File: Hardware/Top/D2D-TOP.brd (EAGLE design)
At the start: 38 x 38 mm, 54 parts, among them SW1 SWITCH.MOM, SW2 SWITCH.MOM, U2 NRF52832_MODULE_MDBT42, U4 PCF8523, U6 PHOTOTRANSISTOR

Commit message: current top and bottom board
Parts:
- added SW5: SWITCH.MOM, LinnesLab-Switches:TACTILE_SWITCH_SMD_6.2MM_TALL
- moved C16 18.7 mm to (9.37, 21.7)
- moved U4 13.0 mm to (7.32, 15.8)
- moved XTAL3 11.8 mm to (5.33, 21.4)
- moved C2 11.1 mm to (5.28, 24.8), turned to 91.7 degrees
- moved C18 11.0 mm to (13.1, 23.7)
- moved L2 10.9 mm to (10.2, 26.1)
- moved C17 10.5 mm to (5.23, 31.8)
- moved C12 10.3 mm to (12.7, 20.4)
- moved C4 10.0 mm to (8.31, 28.4)
- moved C7 10.0 mm to (12.7, 27.5)
- moved C19 6.95 mm to (5.28, 28.1)
- moved R16 5.59 mm to (12.4, 30.0)
- moved U6 5.27 mm to (12.9, 33.0)
- moved C5 5.10 mm to (9.14, 2.97)
- moved R8 4.65 mm to (7.47, 32.2)
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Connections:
- net VBATT renamed VBAT
- net GND: now also SW5.B1, SW5.B2, USB2.S1, USB2.S2, USB2.S3, USB2.S4, USB2.S5, USB2.S6
- net SW1: now also SW5.A1

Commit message: unfinished 002
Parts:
- removed SW5: SWITCH.MOM, LinnesLab-Switches:TACTILE_SWITCH_SMD_6.2MM_TALL
- added C23: 100n, LinnesLab-Passives:C0603
- added C24, C25: 47p, LinnesLab-Passives:C0603
- added J1: (no value), LinnesLab-Connectors:1X07
- added JP2: (no value), LinnesLab-Switches:SMT-JUMPER_2_NO_SILK
- added LED5: RED, LinnesLab-LED:LED-0603
- added LED6: YELLOW, LinnesLab-LED:LED-0603
- added R1, R2: 0, LinnesLab-Passives:R0603
- added R18, R19: 27, LinnesLab-Passives:R0603
- added R20, R21: 1k, LinnesLab-Passives:R0603
- added U5: FT231XS, LinnesLab-DigitalIC:SSOP20_L
- R9: value 10k -> (none)
- moved R9 45.8 mm to (-3.58, -11.9), turned to 0 degrees
- moved R8 42.8 mm to (-3.58, -9.17), turned to 0 degrees
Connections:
- removed net BATT: R13.1, R14.2
- removed net CHRG.STAT: CHRG2.1, R12.1
- removed net RXD: U2.21
- removed net TXD: U2.19
- new net A4/BATT: R13.1, R14.2, U2.5
- new net CTS: JP2.2, U5.9
- new net D27/CHRGSTATUS: CHRG2.1, R12.1, U2.4
- new net FT3V3: U5.13
- new net N$23: R18.2, U5.12
- new net N$24: R19.2, U5.11
- new net N$25: LED5.C, R20.2
- new net N$26: LED6.C, R21.2
- new net RXD.FT: R2.1, U5.4
- new net RXD.NRF: R1.2, U2.21
- new net RXLED: R20.1, U5.17
- new net TXD.FT: R1.1, U5.20
- new net TXD.NRF: R2.2, U2.19
- new net TXLED: R21.1, U5.10
- net 3.3V: now also C23.2, LED5.A, LED6.A, U5.14, U5.3
- net DTR: now also U5.1
- net GND: now also C23.1, C24.2, C25.1, JP2.1, U5.16, U5.6; no longer SW5.B1, SW5.B2
- net SCL: now also R9.1; no longer R8.1
- net SDA: now also R8.1; no longer R9.1
- net SW1: no longer SW5.A1
- net USB+: now also C24.1, R19.1
- net USB-: now also C25.2, R18.1
- net V_USB: now also U5.15

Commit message: updated to 002
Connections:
- removed net CD1: SD2.CD1
- removed net CS.OLED: U3.13
- removed net DC.OLED: U3.15
- removed net RESET.OLED: U3.14
- removed net SD.CS: SD2.2
- removed net SW1: SW1.A1, SW2.A1
- new net A6/TIA: J1.5, U2.7
- new net A7/PPG: J1.7, U2.8
- new net D11/SW1: SW1.A1, U2.25
- new net D15/SW2: SW2.A1, U2.29
- new net D16/CS.OLED: U2.30, U3.13
- new net D29/LED.CTRL: J1.6, U2.6
- new net D3/RESET.OLED: U2.16, U3.14
- new net D4/DC.OLED: U2.17, U3.15
- new net D5/CD1: SD2.CD1, U2.18
- new net D7/SD.CS: SD2.2, U2.20
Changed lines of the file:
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@@
 <contactref element="U2" pad="38"/>
-</signal>
-<signal name="DC.OLED">
-<contactref element="U3" pad="15"/>
-</signal>
-<signal name="RESET.OLED">
-<contactref element="U3" pad="14"/>
 </signal>
 <signal name="N$1">
@@
 <wire x1="17.1766" y1="31.799" x2="13.0556" y2="24.3228" width="0" layer="19" extent="1-1"/>
 </signal>
-<signal name="CS.OLED">
-<contactref element="U3" pad="13"/>
-</signal>
 <signal name="CD2">
 <contactref element="SD2" pad="CD2"/>
-</signal>
-<signal name="CD1">
-<contactref element="SD2" pad="CD1"/>
-</signal>
-<signal name="SD.CS">
-<contactref element="SD2" pad="2"/>
 </signal>
 <signal name="N$17">
@@
 <wire x1="7.4558" y1="28.3972" x2="11.5706" y2="30.0482" width="0" layer="19" extent="1-1"/>
 </signal>
-<signal name="SW1">
-<contactref element="SW1" pad="A1"/>
-<contactref element="SW2" pad="A1"/>
-<wire x1="28.0798" y1="2.0426" x2="27.8766" y2="8.6466" width="0" layer="19" extent="1-1"/>
-</signal>
 <signal name="VBAT">
 <contactref element="U4" pad="3"/>
@@
 <wire x1="7.3406" y1="8.9272" x2="10.033" y2="7.1002" width="0" layer="19" extent="1-1"/>
 </signal>
+<signal name="D7/SD.CS">
+<contactref element="U2" pad="20"/>
+<contactref element="SD2" pad="2"/>
+<wire x1="31.2204" y1="7.3908" x2="32.007" y2="20.8488" width="0" layer="19" extent="1-16"/>
+</signal>
+<signal name="D5/CD1">
+<contactref element="U2" pad="18"/>
+<contactref element="SD2" pad="CD1"/>
+<wire x1="21.4204" y1="13.2908" x2="30.607" y2="20.8488" width="0" layer="19" extent="1-16"/>
+</signal>
+<signal name="D11/SW1">
+<contactref element="U2" pad="25"/>
+<contactref element="SW1" pad="A1"/>
+<wire x1="28.0798" y1="2.0426" x2="35.207" y2="22.2988" width="0" layer="19" extent="1-1"/>
+</signal>
+<signal name="D15/SW2">
+<contactref element="U2" pad="29"/>
+<contactref element="SW2" pad="A1"/>
+<wire x1="27.8766" y1="8.6466" x2="35.207" y2="25.0988" width="0" layer="19" extent="1-1"/>
+</signal>
+<signal name="D16/CS.OLED">
+<contactref element="U2" pad="30"/>
+<contactref element="U3" pad="13"/>
+<wire x1="17.1766" y1="21.999" x2="35.207" y2="25.7988" width="0" layer="19" extent="1-1"/>
+</signal>
+<signal name="D4/DC.OLED">
+<contactref element="U2" pad="17"/>
+<contactref element="U3" pad="15"/>
+<wire x1="17.1766" y1="23.399" x2="29.907" y2="20.8488" width="0" layer="19" extent="1-1"/>
+</signal>
+<signal name="D3/RESET.OLED">
+<contactref element="U2" pad="16"/>
+<contactref element="U3" pad="14"/>
+<wire x1="17.1766" y1="22.699" x2="29.207" y2="20.8488" width="0" layer="19" extent="1-1"/>
+</signal>
+<signal name="D29/LED.CTRL">
+<contactref element="U2" pad="6"/>
+<contactref element="J1" pad="6"/>
+<wire x1="17.7" y1="33" x2="26.007" y2="26.4988" width="0" layer="19" extent="1-1"/>
+</signal>
+<signal name="A6/TIA">
+<contactref element="U2" pad="7"/>
+<contactref element="J1" pad="5"/>
+<wire x1="15.16" y1="33" x2="26.007" y2="25.7988" width="0" layer="19" extent="1-1"/>
+</signal>
+<signal name="A7/PPG">
+<contactref element="U2" pad="8"/>
+<contactref element="J1" pad="7"/>
+<wire x1="20.24" y1="33" x2="26.007" y2="25.0988" width="0" layer="19" extent="1-1"/>
+</signal>
 </signals>

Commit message: checkpoint 3
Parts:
- removed CHRG2: MCP73831, LinnesLab-Power:SOT23-5
- added CHRG: MCP73831, LinnesLab-Power:SOT23-5
- J1: device LinnesLab-Connectors:1X07 -> LinnesLab-Connectors:1X07_1.27MM
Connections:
- net 3.3V: now also J1.4
- net A6/TIA: now also J1.6; no longer J1.5
- net D27/CHRGSTATUS: now also CHRG.1; no longer CHRG2.1
- net D29/LED.CTRL: now also J1.5; no longer J1.6
- net GND: now also CHRG.2, J1.3; no longer CHRG2.2
- net N$17: now also CHRG.5; no longer CHRG2.5
- net SCL: now also J1.2
- net SDA: now also J1.1
- net VIN: now also CHRG.4; no longer CHRG2.4
- net VLIPO: now also CHRG.3; no longer CHRG2.3
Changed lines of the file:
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@@
 <attribute name="VALUE" x="19.0246" y="10.0838" size="1.27" layer="27" rot="R270"/>
 </element>
-<element name="CHRG2" library="LinnesLab-Power" package="SOT23-5" value="MCP73831" x="17.8054" y="9.525" smashed="yes" rot="R270">
-<attribute name="NAME" x="14.6812" y="11.7094" size="0.6604" layer="25" ratio="20" align="bottom-center"/>
-<attribute name="PROD_ID" value="IC-09995" x="3.8354" y="-6.985" size="1.778" layer="27" rot="R270" display="off"/>
-<attribute name="VALUE" x="17.8054" y="6.985" size="0.6604" layer="27" ratio="20" align="bottom-center"/>
+<element name="CHRG" library="LinnesLab-Power" package="SOT23-5" value="MCP73831" x="18.1356" y="-6.223" smashed="yes" rot="R270">
+<attribute name="NAME" x="15.0114" y="-4.0386" size="0.6604" layer="25" ratio="20" align="bottom-center"/>
+<attribute name="PROD_ID" value="IC-09995" x="4.1656" y="-22.733" size="1.778" layer="27" rot="R270" display="off"/>
+<attribute name="VALUE" x="18.1356" y="-8.763" size="0.6604" layer="27" ratio="20" align="bottom-center"/>
 </element>
 <element name="D4" library="LinnesLab-DiscreteSemi" package="USC" package3d_urn="urn:adsk.eagle:package:15664784/2" value="" x="2.6924" y="7.0612" smashed="yes">
@@
 <attribute name="VALUE" x="-4.2164" y="-13.7668" size="0.7112" layer="27"/>
 </element>
-<element name="J1" library="LinnesLab-Connectors" package="1X07" value="" x="5" y="33" smashed="yes">
-<attribute name="NAME" x="3.73" y="34.397" size="0.6096" layer="25" font="vector" ratio="20"/>
-<attribute name="VALUE" x="3.73" y="30.968" size="0.6096" layer="27" font="vector" ratio="20"/>
+<element name="J1" library="LinnesLab-Connectors" package="1X07_1.27MM" value="" x="5" y="33" locked="yes" smashed="yes">
+<attribute name="NAME" x="4.619" y="34.143" locked="yes" size="0.7112" layer="25"/>
+<attribute name="VALUE" x="4.492" y="31.095" locked="yes" size="0.7112" layer="27" ratio="20"/>
 </element>
 </elements>
@@
 <contactref element="J2" pad="1"/>
 <contactref element="R14" pad="1"/>
-<contactref element="CHRG2" pad="2"/>
+<contactref element="CHRG" pad="2"/>
 <contactref element="R15" pad="1"/>
 <contactref element="C2" pad="2"/>
@@
 <contactref element="U5" pad="6"/>
 <contactref element="U5" pad="16"/>
+<contactref element="J1" pad="3"/>
 <wire x1="30.2632" y1="46.7868" x2="28.5632" y2="51.8668" width="0" layer="19" extent="1-1"/>
 <wire x1="25.1333" y1="46.8503" x2="30.2632" y2="46.7868" width="0" layer="19" extent="1-1"/>
@@
 <wire x1="5.25798125" y1="25.690825" x2="5.2832" y2="28.717" width="0" layer="19" extent="1-1"/>
 <wire x1="5.2324" y1="32.4" x2="5.2832" y2="28.717" width="0" layer="19" extent="1-1"/>
+<wire x1="7.54" y1="33" x2="5.2324" y2="32.4" width="0" layer="19" extent="1-1"/>
 <wire x1="17.1766" y1="21.299" x2="13.0556" y2="23.0228" width="0" layer="19" extent="1-1"/>
 <wire x1="17.1766" y1="19.899" x2="17.1766" y2="21.299" width="0" layer="19" extent="1-1"/>
@@
 <wire x1="20.7636" y1="12.1158" x2="17.1766" y2="13.599" width="0" layer="19" extent="1-1"/>
 <wire x1="20.9296" y1="10.2988" x2="20.7636" y2="12.1158" width="0" layer="19" extent="1-1"/>
-<wire x1="16.5053" y1="9.525" x2="17.1766" y2="13.599" width="0" layer="19" extent="1-1"/>
-<wire x1="12.827" y1="9.1558" x2="16.5053" y2="9.525" width="0" layer="19" extent="1-1"/>
+<wire x1="16.8355" y1="-6.223" x2="17.1766" y2="13.599" width="0" layer="19" extent="1-1"/>
+<wire x1="12.827" y1="9.1558" x2="16.8355" y2="-6.223" width="0" layer="19" extent="1-1"/>
 <wire x1="24.9818" y1="15.2146" x2="20.7636" y2="12.1158" width="0" layer="19" extent="1-1"/>
 <wire x1="27.8766" y1="13.1466" x2="24.9818" y2="15.2146" width="0" layer="19" extent="1-1"/>
@@
 <contactref element="R8" pad="2"/>
 <contactref element="R9" pad="2"/>
+<contactref element="J1" pad="4"/>
 <wire x1="30.2632" y1="51.8668" x2="32.3716" y2="51.6128" width="0" layer="19" extent="1-1"/>
 <wire x1="32.3716" y1="47.8028" x2="32.3716" y2="51.6128" width="0" layer="19" extent="1-1"/>
@@
 <wire x1="19.7739" y1="48.1203" x2="25.1333" y2="45.5803" width="0" layer="19" extent="1-1"/>
 <wire x1="13.7024" y1="32.9946" x2="19.7739" y2="48.1203" width="0" layer="19" extent="1-1"/>
-<wire x1="5.2324" y1="31.1" x2="13.7024" y2="32.9946" width="0" layer="19" extent="1-1"/>
+<wire x1="8.81" y1="33" x2="13.7024" y2="32.9946" width="0" layer="19" extent="1-1"/>
+<wire x1="5.2324" y1="31.1" x2="8.81" y2="33" width="0" layer="19" extent="1-1"/>
 <wire x1="5.2832" y1="27.417" x2="5.2324" y2="31.1" width="0" layer="19" extent="1-1"/>
 <wire x1="5.308415625" y1="23.991571875" x2="5.2832" y2="27.417" width="0" layer="19" extent="1-1"/>
@@
 <contactref element="U4" pad="5"/>
 <contactref element="R8" pad="1"/>
-<wire x1="9.9652" y1="13.9192" x2="26.007" y2="29.2988" width="0" layer="19" extent="1-1"/>
+<contactref element="J1" pad="1"/>
+<wire x1="5" y1="33" x2="26.007" y2="29.2988" width="0" layer="19" extent="1-1"/>
+<wire x1="9.9652" y1="13.9192" x2="5" y2="33" width="0" layer="19" extent="1-1"/>
 <wire x1="-4.4314" y1="-9.1694" x2="9.9652" y2="13.9192" width="0" layer="19" extent="1-1"/>
 </signal>
@@
 <contactref element="U4" pad="6"/>
 <contactref element="R9" pad="1"/>
-<wire x1="9.9652" y1="15.1892" x2="26.007" y2="28.5988" width="0" layer="19" extent="1-1"/>
+<contactref element="J1" pad="2"/>
+<wire x1="6.27" y1="33" x2="26.007" y2="28.5988" width="0" layer="19" extent="1-1"/>
+<wire x1="9.9652" y1="15.1892" x2="6.27" y2="33" width="0" layer="19" extent="1-1"/>
 <wire x1="-4.4314" y1="-11.8618" x2="9.9652" y2="15.1892" width="0" layer="19" extent="1-1"/>
 </signal>
@@
 </signal>
 <signal name="N$17">
-<contactref element="CHRG2" pad="5"/>
+<contactref element="CHRG" pad="5"/>
 <contactref element="R11" pad="2"/>
-<wire x1="19.0636" y1="12.1158" x2="19.1055" y2="10.475" width="0" layer="19" extent="1-1"/>
+<wire x1="19.0636" y1="12.1158" x2="19.4357" y2="-5.273" width="0" layer="19" extent="1-1"/>
 </signal>
 <signal name="VLIPO">
 <contactref element="J2" pad="2"/>
 <contactref element="D4" pad="+"/>
-<contactref element="CHRG2" pad="3"/>
+<contactref element="CHRG" pad="3"/>
 <contactref element="C20" pad="1"/>
 <contactref element="R13" pad="2"/>
-<wire x1="12.827" y1="7.4558" x2="16.5053" y2="8.575" width="0" layer="19" extent="1-1"/>
+<wire x1="12.827" y1="7.4558" x2="16.8355" y2="-7.173" width="0" layer="19" extent="1-1"/>
 <wire x1="10.033" y1="8.8002" x2="12.827" y2="7.4558" width="0" layer="19" extent="1-1"/>
 <wire x1="1.5424" y1="7.0612" x2="12.827" y2="7.4558" width="0" layer="19" extent="1-1"/>
@@
 <contactref element="LDO2" pad="3"/>
 <contactref element="D5" pad="-"/>
-<contactref element="CHRG2" pad="4"/>
+<contactref element="CHRG" pad="4"/>
 <contactref element="C21" pad="2"/>
 <contactref element="R12" pad="2"/>
-<wire x1="19.1055" y1="8.575" x2="20.9296" y2="8.5988" width="0" layer="19" extent="1-1"/>
-<wire x1="18.6808" y1="6.604" x2="19.1055" y2="8.575" width="0" layer="19" extent="1-1"/>
+<wire x1="19.4357" y1="-7.173" x2="20.9296" y2="8.5988" width="0" layer="19" extent="1-1"/>
+<wire x1="18.6808" y1="6.604" x2="19.4357" y2="-7.173" width="0" layer="19" extent="1-1"/>
 <wire x1="15.9973" y1="3.3884" x2="18.6808" y2="6.604" width="0" layer="19" extent="1-1"/>
 <wire x1="9.144" y1="3.8218" x2="15.9973" y2="3.3884" width="0" layer="19" extent="1-1"/>
@@
 <contactref element="U2" pad="4"/>
 <contactref element="R12" pad="1"/>
-<contactref element="CHRG2" pad="1"/>
-<wire x1="16.5053" y1="10.475" x2="26.007" y2="27.8988" width="0" layer="19" extent="1-1"/>
-<wire x1="16.9808" y1="6.604" x2="16.5053" y2="10.475" width="0" layer="19" extent="1-1"/>
+<contactref element="CHRG" pad="1"/>
+<wire x1="16.8355" y1="-5.273" x2="26.007" y2="27.8988" width="0" layer="19" extent="1-1"/>
+<wire x1="16.9808" y1="6.604" x2="16.8355" y2="-5.273" width="0" layer="19" extent="1-1"/>
 </signal>
 <signal name="A4/BATT">
@@
 <signal name="D29/LED.CTRL">
 <contactref element="U2" pad="6"/>
-<contactref element="J1" pad="6"/>
-<wire x1="17.7" y1="33" x2="26.007" y2="26.4988" width="0" layer="19" extent="1-1"/>
+<contactref element="J1" pad="5"/>
+<wire x1="10.08" y1="33" x2="26.007" y2="26.4988" width="0" layer="19" extent="1-1"/>
 </signal>
 <signal name="A6/TIA">
 <contactref element="U2" pad="7"/>
-<contactref element="J1" pad="5"/>
-<wire x1="15.16" y1="33" x2="26.007" y2="25.7988" width="0" layer="19" extent="1-1"/>
+<contactref element="J1" pad="6"/>
+<wire x1="11.35" y1="33" x2="26.007" y2="25.7988" width="0" layer="19" extent="1-1"/>
 </signal>
 <signal name="A7/PPG">
 <contactref element="U2" pad="8"/>
 <contactref element="J1" pad="7"/>
-<wire x1="20.24" y1="33" x2="26.007" y2="25.0988" width="0" layer="19" extent="1-1"/>
+<wire x1="12.62" y1="33" x2="26.007" y2="25.0988" width="0" layer="19" extent="1-1"/>
 </signal>
 </signals>

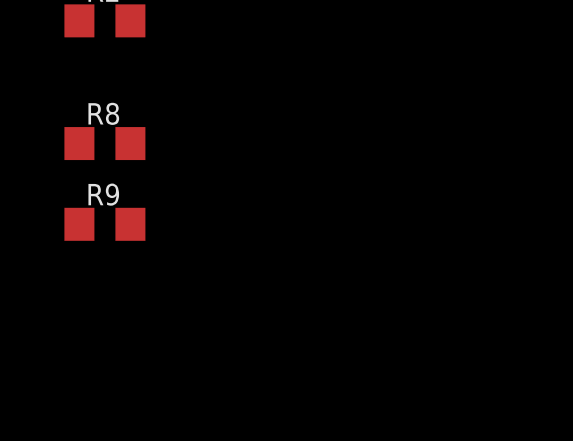
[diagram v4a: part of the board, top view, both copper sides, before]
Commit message: added starting code
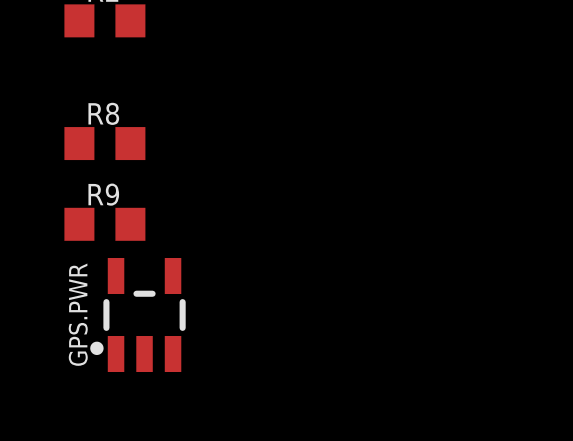
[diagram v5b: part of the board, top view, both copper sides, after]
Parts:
- added GPS.PWR: MIC5504, LinnesLab-Power:SOT23-5
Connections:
- new net D2/GPS.PWR: GPS.PWR.3, U2.15
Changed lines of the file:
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@@
 <attribute name="VALUE" x="4.492" y="31.095" locked="yes" size="0.7112" layer="27" ratio="20"/>
+</element>
+<element name="GPS.PWR" library="LinnesLab-Power" package="SOT23-5" value="MIC5504" x="-2.2606" y="-14.8844" smashed="yes">
+<attribute name="NAME" x="-4.1656" y="-14.8844" size="0.6096" layer="25" ratio="20" rot="R90" align="bottom-center"/>
+<attribute name="VALUE" x="0.2794" y="-14.8844" size="0.6096" layer="27" ratio="20" rot="R90" align="bottom-center"/>
 </element>
 </elements>
@@
 <wire x1="12.62" y1="33" x2="26.007" y2="25.0988" width="0" layer="19" extent="1-1"/>
 </signal>
+<signal name="D2/GPS.PWR">
+<contactref element="U2" pad="15"/>
+<contactref element="GPS.PWR" pad="3"/>
+<wire x1="-1.3106" y1="-16.1845" x2="28.507" y2="20.8488" width="0" layer="19" extent="1-1"/>
+</signal>
 </signals>

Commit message: updated top board
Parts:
- U4: value PCF8523 -> FT231XS; device LinnesLab-Clocks:SO8 -> LinnesLab-DigitalIC:SSOP20_L
- U5: value FT231XS -> PCF8523; device LinnesLab-DigitalIC:SSOP20_L -> LinnesLab-Clocks:SO8
- moved R1 76.9 mm to (49.6, 53.2)
- moved R2 75.9 mm to (44.7, 53.4)
- moved U5 55.4 mm to (74.3, 27.0), turned to 0 degrees
- moved C16 51.3 mm to (60.4, 16.4)
- moved C19 51.3 mm to (56.3, 22.7)
- moved C2 51.3 mm to (56.3, 19.5)
- moved C4 51.3 mm to (59.3, 23.0)
- moved R16 51.3 mm to (63.4, 24.7)
- moved U6 51.3 mm to (63.8, 27.6)
- moved XTAL3 51.3 mm to (56.3, 16.1)
- moved C13 51.3 mm to (58.2, 15.8)
- moved C15 51.3 mm to (58.4, 20.5)
- moved LDO2 51.2 mm to (68.5, 4.47)
- moved U4 50.1 mm to (46.0, 47.7), turned to 270 degrees
- moved C17 43.8 mm to (48.7, 37.5)
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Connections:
- net 3.3V: now also U4.14, U4.3, U5.8; no longer U4.8, U5.14, U5.3
- net CTS: now also U4.9; no longer U5.9
- net DTR: now also U4.1; no longer U5.1
- net FT3V3: now also U4.13; no longer U5.13
- net GND: now also U4.16, U4.6, U5.4; no longer U4.4, U5.16, U5.6
- net N$19: now also U5.2; no longer U4.2
- net N$20: now also U5.1; no longer U4.1
- net N$23: now also U4.12; no longer U5.12
- net N$24: now also U4.11; no longer U5.11
- net RXD.FT: now also U4.4; no longer U5.4
- net RXLED: now also U4.17; no longer U5.17
- net SCL: now also U5.6; no longer U4.6
- net SDA: now also U5.5; no longer U4.5
- net TXD.FT: now also U4.20; no longer U5.20
- net TXLED: now also U4.10; no longer U5.10
- net VBAT: now also U5.3; no longer U4.3
- net V_USB: now also U4.15; no longer U5.15
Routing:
- net TXLED: track 0.00 -> 13.5 mm, vias 0 -> 2
- net RXD.FT: track 0.00 -> 6.16 mm
- net N$12: track 0.00 -> 3.71 mm
- net TXD.FT: track 0.00 -> 2.67 mm
- net N$24: track 0.00 -> 2.65 mm
- net N$11: track 0.00 -> 2.39 mm
- net USB+: track 0.00 -> 1.92 mm
- net USB-: track 0.00 -> 1.80 mm
- net N$26: track 0.00 -> 1.67 mm
- net N$25: track 0.00 -> 1.64 mm
- net RXLED: track 0.00 -> 1.62 mm
- net N$23: track 0.00 -> 1.58 mm
- net GND: track 0.00 -> 1.24 mm, vias 0 -> 1

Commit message: completed 004
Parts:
- removed GPS.PWR: MIC5504, LinnesLab-Power:SOT23-5
- moved LDO2 54.5 mm to (14.0, 3.92), flipped to the bottom, turned to 90 degrees
- moved C13 49.9 mm to (8.52, 20.9), turned to 270 degrees
- moved C15 47.9 mm to (10.5, 20.9), turned to 270 degrees
- moved R7 47.0 mm to (31.6, 17.3)
- moved C19 43.9 mm to (12.4, 20.9)
- moved C17 38.5 mm to (13.9, 20.9)
- moved SW1 36.3 mm to (21.7, 4.46)
- moved C6 36.0 mm to (16.7, 3.90), flipped to the bottom, turned to 90 degrees
- moved C16 28.9 mm to (31.6, 19.6), turned to 180 degrees
- moved R6 27.8 mm to (15.4, 21.3), turned to 270 degrees
- moved C5 27.2 mm to (10.8, 4.01), flipped to the bottom, turned to 270 degrees
- moved C2 22.6 mm to (76.1, 30.4), turned to 179.4 degrees
- moved D4 20.9 mm to (9.07, 4.15), flipped to the bottom, turned to 270 degrees
- moved XTAL3 18.2 mm to (69.9, 28.2)
- moved SW2 17.7 mm to (31.7, 4.50)
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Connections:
- removed net D2/GPS.PWR: GPS.PWR.3, U2.15
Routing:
- net GND: track 1.24 -> 28.9 mm, vias 1 -> 16
- net VLIPO: track 0.00 -> 13.3 mm
- net VIN: track 0.00 -> 8.36 mm
- net N$2: track 0.00 -> 6.55 mm
- net 3.3V: track 0.00 -> 5.92 mm, vias 0 -> 1
- net N$13: track 0.00 -> 5.72 mm
- net N$5: track 0.00 -> 3.74 mm
- net N$8: track 0.00 -> 3.72 mm
- net N$15: track 0.00 -> 3.10 mm
- net V_USB: track 0.00 -> 2.52 mm
- net N$1: track 0.00 -> 2.21 mm
- net N$3: track 0.00 -> 2.15 mm
- net N$7: track 0.00 -> 2.01 mm
- net N$19: track 0.00 -> 1.86 mm
- net N$20: track 0.00 -> 1.81 mm
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- added copper zone on layer 1, net 3.3V
- added copper zone on layer 16, net GND
